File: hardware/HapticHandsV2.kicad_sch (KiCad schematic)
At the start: 6 parts, among them J6 DEBUG, U1 STM32F411RETx

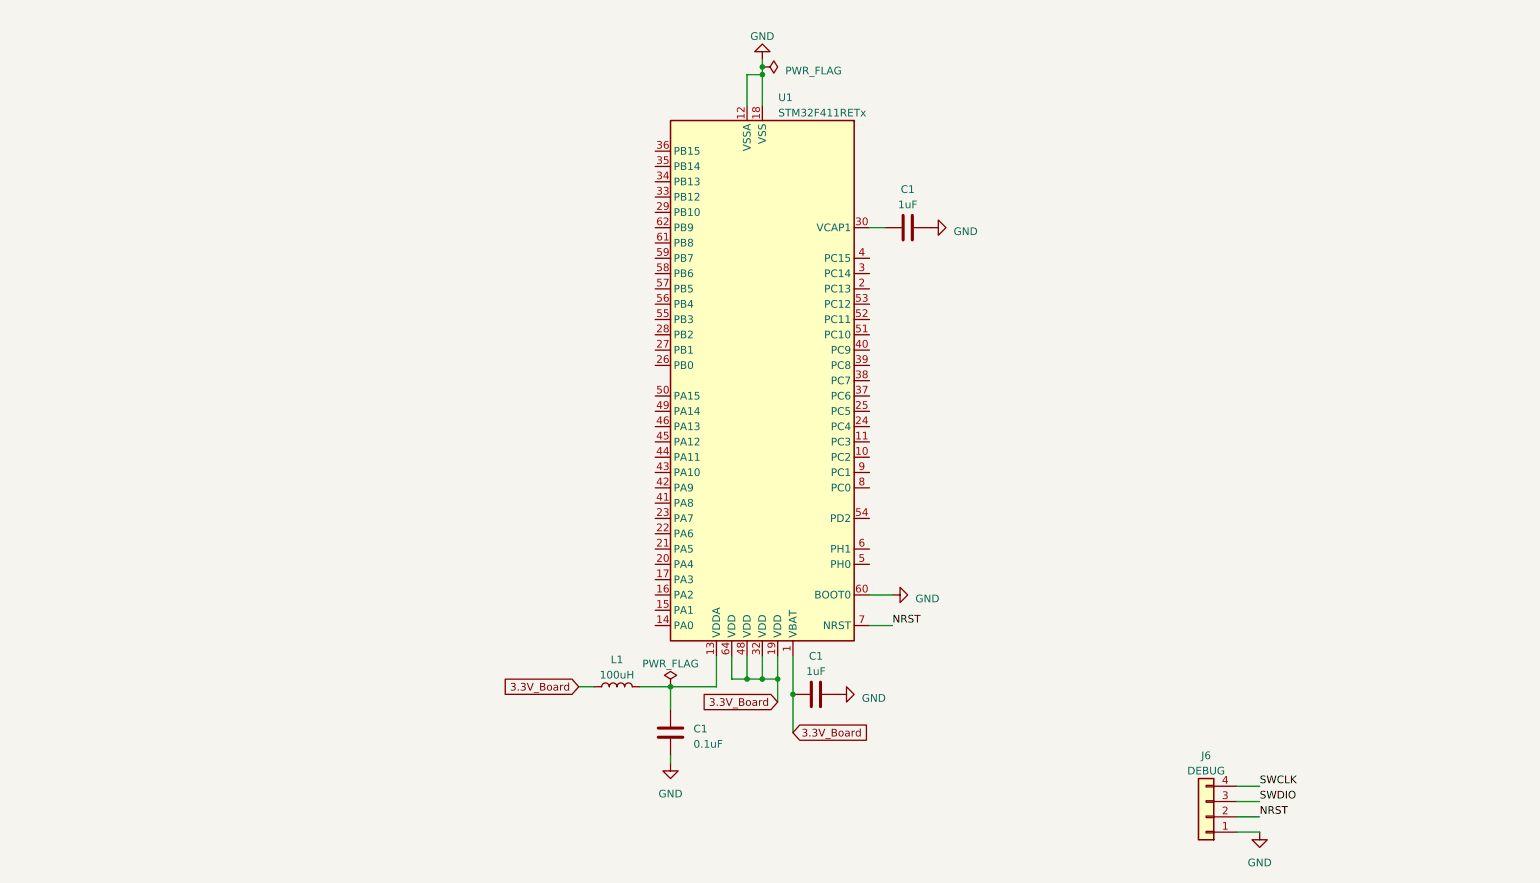
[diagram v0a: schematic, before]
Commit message: Setup STM32F411 .ioc file (timers, pwm, adc pin, etc). Made progress on PCB circuit design.
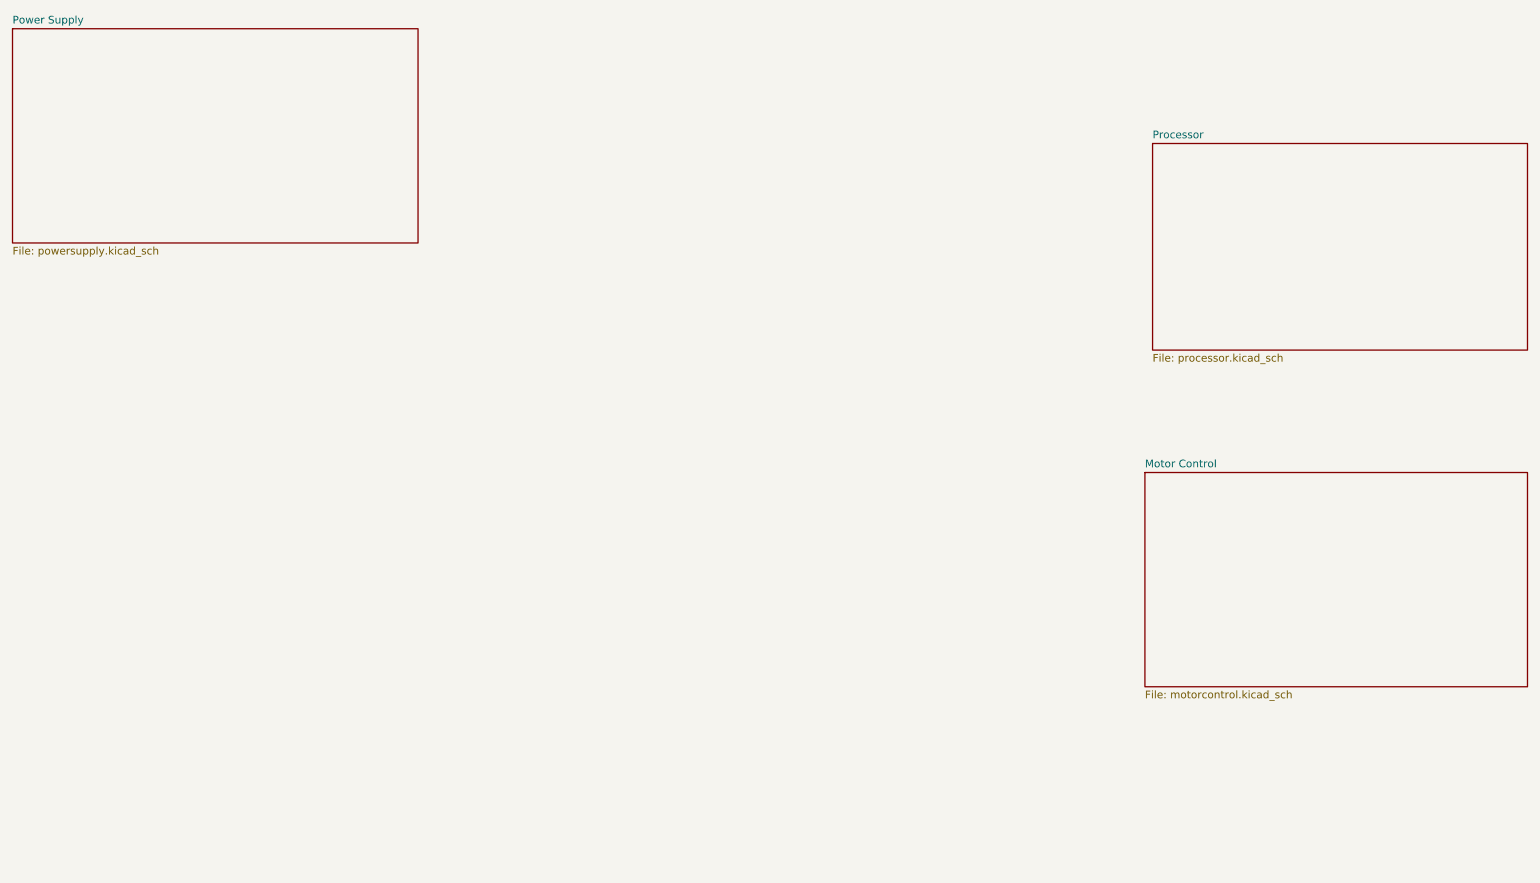
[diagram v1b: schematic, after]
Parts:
- removed C1 (x2): 1uF, Capacitor_SMD:C_0402_1005Metric, symbol Device:C
- removed C1: 0.1uF, Capacitor_SMD:C_0402_1005Metric, symbol Device:C
- removed J6: DEBUG, Connector_JST:JST_PH_B4B-PH-K_1x04_P2.00mm_Vertical, symbol Connector_Generic:Conn_01x04
- removed L1: 100uH, Inductor_SMD:L_0805_2012Metric, symbol Device:L
- removed U1: STM32F411RETx, Package_QFP:LQFP-64_10x10mm_P0.5mm, symbol MCU_ST_STM32F4:STM32F411RETx
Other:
- added sheet Motor Control (motorcontrol.kicad_sch)
- added sheet Power Supply (powersupply.kicad_sch)
- added sheet Processor (processor.kicad_sch)

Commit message: Change STM code to support an I2C bus. Add encoder reading code - tested on TIM1.
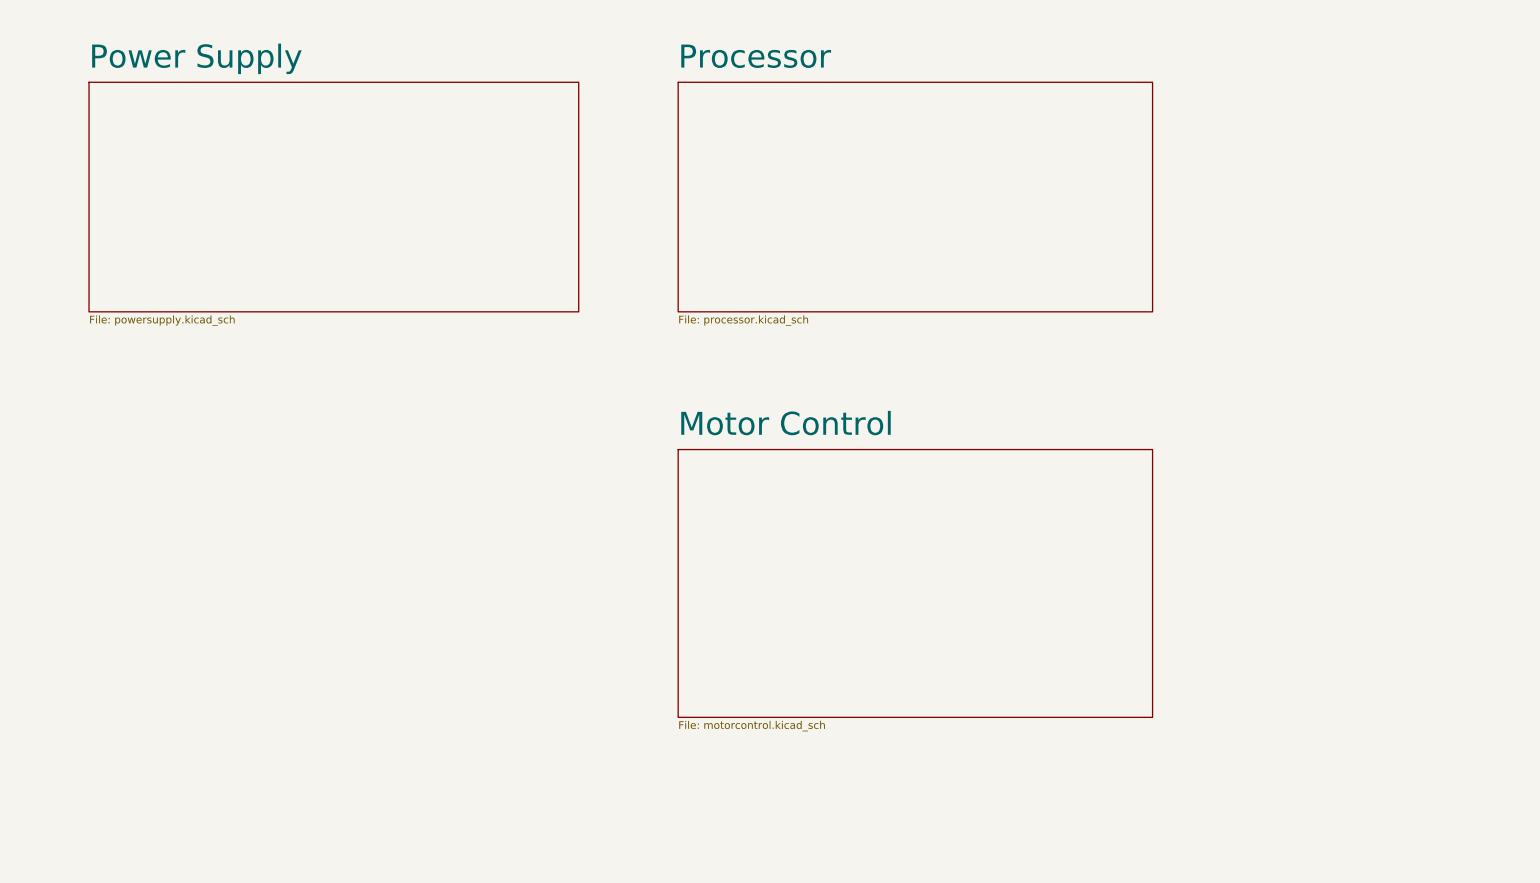
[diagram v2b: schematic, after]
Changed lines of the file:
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@@
 (kicad_sch (version 20230121) (generator eeschema)
   (paper "A4")
-  (sheet (at 204.47 96.52) (size 63.5 35.56) (fields_autoplaced)
+  (sheet (at 127 92.71) (size 78.74 44.45) (fields_autoplaced)
     (stroke (width 0.1524) (type solid))
     (fill (color 0 0 0 0.0000))
-    (property "Sheetname" "Motor Control" (at 204.47 95.8084 0)
-      (effects (font (size 1.27 1.27)) (justify left bottom))
+    (property "Sheetname" "Motor Control" (at 127 90.7284 0)
+      (effects (font (size 3.81 3.81)) (justify left bottom))
     )
-    (property "Sheetfile" "motorcontrol.kicad_sch" (at 204.47 132.6646 0)
+    (property "Sheetfile" "motorcontrol.kicad_sch" (at 127 137.7446 0)
       (effects (font (size 1.27 1.27)) (justify left top))
     )
@@
     )
   )
-  (sheet (at 205.74 41.91) (size 62.23 34.29) (fields_autoplaced)
+  (sheet (at 127 31.75) (size 78.74 38.1) (fields_autoplaced)
     (stroke (width 0.1524) (type solid))
     (fill (color 0 0 0 0.0000))
-    (property "Sheetname" "Processor" (at 205.74 41.1984 0)
-      (effects (font (size 1.27 1.27)) (justify left bottom))
+    (property "Sheetname" "Processor" (at 127 29.7684 0)
+      (effects (font (size 3.81 3.81)) (justify left bottom))
     )
-    (property "Sheetfile" "processor.kicad_sch" (at 205.74 76.7846 0)
+    (property "Sheetfile" "processor.kicad_sch" (at 127 70.4346 0)
       (effects (font (size 1.27 1.27)) (justify left top))
     )
@@
     )
   )
-  (sheet (at 16.51 22.86) (size 67.31 35.56) (fields_autoplaced)
+  (sheet (at 29.21 31.75) (size 81.28 38.1) (fields_autoplaced)
     (stroke (width 0.1524) (type solid))
     (fill (color 0 0 0 0.0000))
-    (property "Sheetname" "Power Supply" (at 16.51 22.1484 0)
-      (effects (font (size 1.27 1.27)) (justify left bottom))
+    (property "Sheetname" "Power Supply" (at 29.21 29.7684 0)
+      (effects (font (size 3.81 3.81)) (justify left bottom))
     )
-    (property "Sheetfile" "powersupply.kicad_sch" (at 16.51 59.0046 0)
+    (property "Sheetfile" "powersupply.kicad_sch" (at 29.21 70.4346 0)
       (effects (font (size 1.27 1.27)) (justify left top))
     )
